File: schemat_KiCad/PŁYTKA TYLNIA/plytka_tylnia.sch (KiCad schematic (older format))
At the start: 58 parts, among them J1 CONN_01X04, J2 PIN8, J3 PIN8, P1 USB_OTG

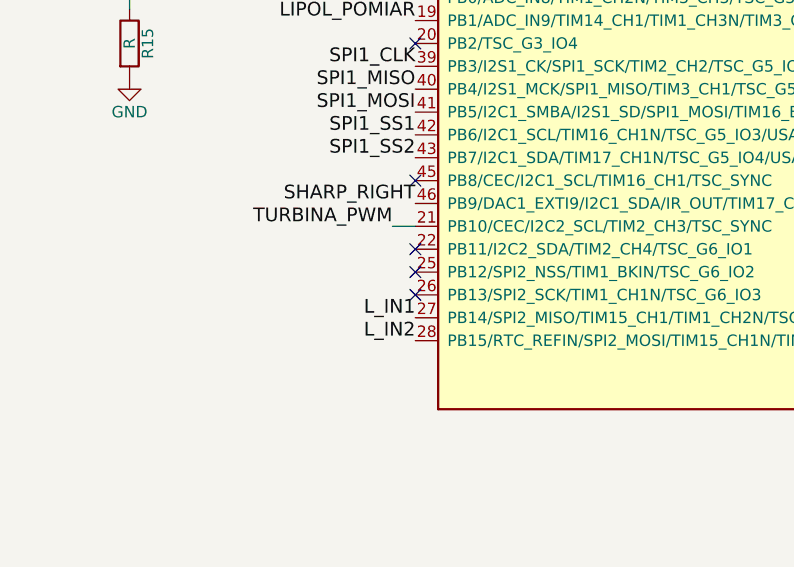
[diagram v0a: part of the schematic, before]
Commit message: kondensatory spolaryzowane na tantalowe
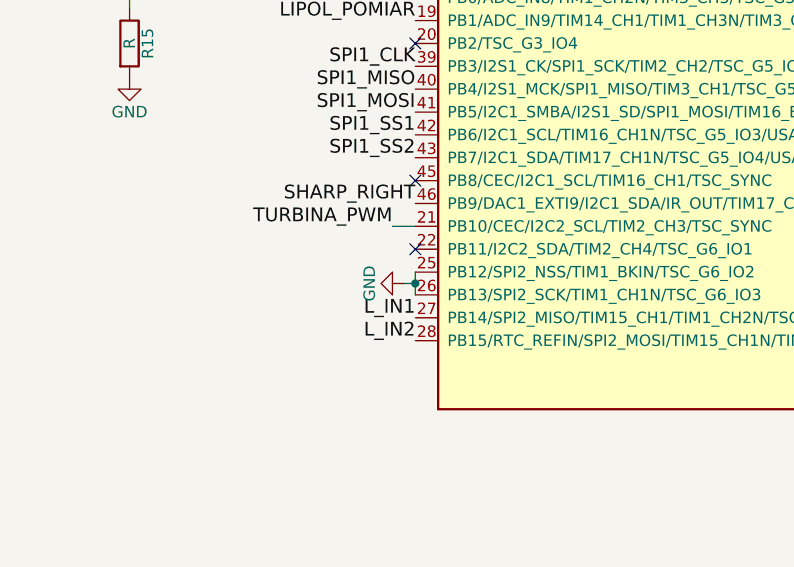
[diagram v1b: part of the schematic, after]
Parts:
- C1, C10, C14, C15, C16, C7, C8, C9: footprint Capacitors_SMD:C_0805_HandSoldering -> Capacitors_Tantalum_SMD:CP_Tantalum_Case-A_EIA-3216-18_Hand
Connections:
- net GND: now also MIKROPROCEK1.25 (PB12/SPI2_NSS/TIM1_BKIN/TSC_G6_IO2), MIKROPROCEK1.26 (PB13/SPI2_SCK/TIM1_CH1N/TSC_G6_IO3)
- no-connect marks 8 -> 6
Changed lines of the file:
@@
 F 0 "C7" H 5675 1200 50  0000 L CNN
 F 1 "4,7uF" H 5675 1000 50  0000 L CNN
-F 2 "Capacitors_SMD:C_0805_HandSoldering" H 5688 950 50  0001 C CNN
+F 2 "Capacitors_Tantalum_SMD:CP_Tantalum_Case-A_EIA-3216-18_Hand" H 5688 950 50  0001 C CNN
 F 3 "" H 5650 1100 50  0000 C CNN
 	1    5650 1100
@@
 F 0 "C10" H 12975 1250 50  0000 L CNN
 F 1 "1uF" H 12975 1050 50  0000 L CNN
-F 2 "Capacitors_SMD:C_0805_HandSoldering" H 12988 1000 50  0001 C CNN
+F 2 "Capacitors_Tantalum_SMD:CP_Tantalum_Case-A_EIA-3216-18_Hand" H 12988 1000 50  0001 C CNN
 F 3 "" H 12950 1150 50  0000 C CNN
 	1    12950 1150
@@
 F 0 "C9" H 15125 8200 50  0000 L CNN
 F 1 "10uF" H 15125 8000 50  0000 L CNN
-F 2 "Capacitors_SMD:C_0805_HandSoldering" H 15138 7950 50  0001 C CNN
+F 2 "Capacitors_Tantalum_SMD:CP_Tantalum_Case-A_EIA-3216-18_Hand" H 15138 7950 50  0001 C CNN
 F 3 "" H 15100 8100 50  0000 C CNN
 	1    15100 8100
@@
 F 0 "C8" H 14025 8250 50  0000 L CNN
 F 1 "10uF" H 14025 8050 50  0000 L CNN
-F 2 "Capacitors_SMD:C_0805_HandSoldering" H 14038 8000 50  0001 C CNN
+F 2 "Capacitors_Tantalum_SMD:CP_Tantalum_Case-A_EIA-3216-18_Hand" H 14038 8000 50  0001 C CNN
 F 3 "" H 14000 8150 50  0000 C CNN
 	1    14000 8150
@@
 F 0 "C14" H 15325 1350 50  0000 L CNN
 F 1 "10uF" H 15325 1150 50  0000 L CNN
-F 2 "Capacitors_SMD:C_0805_HandSoldering" H 15338 1100 50  0001 C CNN
+F 2 "Capacitors_Tantalum_SMD:CP_Tantalum_Case-A_EIA-3216-18_Hand" H 15338 1100 50  0001 C CNN
 F 3 "" H 15300 1250 50  0000 C CNN
 	1    15300 1250
@@
 F 0 "C16" H 15125 6950 50  0000 L CNN
 F 1 "10uF" H 15125 6750 50  0000 L CNN
-F 2 "Capacitors_SMD:C_0805_HandSoldering" H 15138 6700 50  0001 C CNN
+F 2 "Capacitors_Tantalum_SMD:CP_Tantalum_Case-A_EIA-3216-18_Hand" H 15138 6700 50  0001 C CNN
 F 3 "" H 15100 6850 50  0000 C CNN
 	1    15100 6850
@@
 F 0 "C15" H 14025 7000 50  0000 L CNN
 F 1 "10uF" H 14025 6800 50  0000 L CNN
-F 2 "Capacitors_SMD:C_0805_HandSoldering" H 14038 6750 50  0001 C CNN
+F 2 "Capacitors_Tantalum_SMD:CP_Tantalum_Case-A_EIA-3216-18_Hand" H 14038 6750 50  0001 C CNN
 F 3 "" H 14000 6900 50  0000 C CNN
 	1    14000 6900
@@
 F 0 "C1" H 5275 1200 50  0000 L CNN
 F 1 "4,7uF" H 5275 1000 50  0000 L CNN
-F 2 "Capacitors_SMD:C_0805_HandSoldering" H 5288 950 50  0001 C CNN
+F 2 "Capacitors_Tantalum_SMD:CP_Tantalum_Case-A_EIA-3216-18_Hand" H 5288 950 50  0001 C CNN
 F 3 "" H 5250 1100 50  0000 C CNN
 	1    5250 1100
@@
 Wire Wire Line
 	3150 9900 3100 9900
-NoConn ~ 2200 5350
-NoConn ~ 2200 5450
 NoConn ~ 2200 4350
 Text Label 2100 5150 2    60   ~ 0
@@
 Wire Wire Line
 	12000 7900 12000 8500
+Wire Wire Line
+	2200 5350 2200 5450
+Wire Wire Line
+	2200 5400 2150 5400
+Connection ~ 2200 5400
+$Comp
+L GND #PWR?
+U 1 1 5910F31F
+P 2150 5400
+F 0 "#PWR?" H 2150 5150 50  0001 C CNN
+F 1 "GND" H 2150 5250 50  0000 C CNN
+F 2 "" H 2150 5400 50  0001 C CNN
+F 3 "" H 2150 5400 50  0001 C CNN
+	1    2150 5400
+	0    1    1    0
+$EndComp
 $EndSCHEMATC

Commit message: skompletowane czesci, wybrane rezystory, kondensator przy wejsciu
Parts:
- added C18: 100nF, Capacitors_SMD:C_0805_HandSoldering, symbol C
- C10: value 1uF -> 10uF
- C11: value 10uF -> 100nF
- C13: value 0.1uF -> 100nF
- R10: value R -> 220R
- R11: value R -> 43k
- R12: value R -> 13k
- R13: value R -> 56k
- R14: value R -> 51k
- R15: value R -> 33k
- R4: value R -> 160k
- R5: value R -> 20k
- R9: value R -> 10k
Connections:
- net GND: now also C18.2
- net VCC: now also C18.1
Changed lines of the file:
@@
 P 13200 1150
 F 0 "C11" H 13225 1250 50  0000 L CNN
-F 1 "10uF" H 13225 1050 50  0000 L CNN
+F 1 "100nF" H 13225 1050 50  0000 L CNN
 F 2 "Capacitors_SMD:C_0805_HandSoldering" H 13238 1000 50  0001 C CNN
 F 3 "" H 13200 1150 50  0000 C CNN
@@
 P 12950 1150
 F 0 "C10" H 12975 1250 50  0000 L CNN
-F 1 "1uF" H 12975 1050 50  0000 L CNN
+F 1 "10uF" H 12975 1050 50  0000 L CNN
 F 2 "Capacitors_Tantalum_SMD:CP_Tantalum_Case-A_EIA-3216-18_Hand" H 12988 1000 50  0001 C CNN
 F 3 "" H 12950 1150 50  0000 C CNN
@@
 L VCC #PWR07
 U 1 1 5825FE4C
-P 1750 9800
-F 0 "#PWR07" H 1750 9650 50  0001 C CNN
-F 1 "VCC" H 1750 9950 50  0000 C CNN
-F 2 "" H 1750 9800 50  0000 C CNN
-F 3 "" H 1750 9800 50  0000 C CNN
-	1    1750 9800
+P 1550 9550
+F 0 "#PWR07" H 1550 9400 50  0001 C CNN
+F 1 "VCC" H 1550 9700 50  0000 C CNN
+F 2 "" H 1550 9550 50  0000 C CNN
+F 3 "" H 1550 9550 50  0000 C CNN
+	1    1550 9550
 	1    0    0    -1
 $EndComp
@@
 P 14850 1250
 F 0 "C13" H 14875 1350 50  0000 L CNN
-F 1 "0.1uF" H 14875 1150 50  0000 L CNN
+F 1 "100nF" H 14875 1150 50  0000 L CNN
 F 2 "Capacitors_SMD:C_0805_HandSoldering" H 14888 1100 50  0001 C CNN
 F 3 "" H 14850 1250 50  0000 C CNN
@@
 	1550 9900 2100 9900
 Wire Wire Line
-	1750 9800 1550 9800
-Wire Wire Line
 	12550 1300 12550 1100
 Wire Wire Line
@@
 P 9950 1750
 F 0 "R10" V 10030 1750 50  0000 C CNN
-F 1 "R" V 9950 1750 50  0000 C CNN
+F 1 "220R" V 9950 1750 50  0000 C CNN
 F 2 "Resistors_SMD:R_0805_HandSoldering" V 9880 1750 50  0001 C CNN
 F 3 "" H 9950 1750 50  0001 C CNN
@@
 P 10850 1400
 F 0 "R11" V 10930 1400 50  0000 C CNN
-F 1 "R" V 10850 1400 50  0000 C CNN
+F 1 "43k" V 10850 1400 50  0000 C CNN
 F 2 "Resistors_SMD:R_0805_HandSoldering" V 10780 1400 50  0001 C CNN
 F 3 "" H 10850 1400 50  0001 C CNN
@@
 P 10850 1700
 F 0 "R12" V 10930 1700 50  0000 C CNN
-F 1 "R" V 10850 1700 50  0000 C CNN
+F 1 "13k" V 10850 1700 50  0000 C CNN
 F 2 "Resistors_SMD:R_0805_HandSoldering" V 10780 1700 50  0001 C CNN
 F 3 "" H 10850 1700 50  0001 C CNN
@@
 P 10850 2150
 F 0 "R13" V 10930 2150 50  0000 C CNN
-F 1 "R" V 10850 2150 50  0000 C CNN
+F 1 "56k" V 10850 2150 50  0000 C CNN
 F 2 "Resistors_SMD:R_0805_HandSoldering" V 10780 2150 50  0001 C CNN
 F 3 "" H 10850 2150 50  0001 C CNN
@@
 P 10850 2000
 F 0 "R9" V 10930 2000 50  0000 C CNN
-F 1 "R" V 10850 2000 50  0000 C CNN
+F 1 "10k" V 10850 2000 50  0000 C CNN
 F 2 "Resistors_SMD:R_0805_HandSoldering" V 10780 2000 50  0001 C CNN
 F 3 "" H 10850 2000 50  0001 C CNN
@@
 P 10850 1850
 F 0 "R5" V 10930 1850 50  0000 C CNN
-F 1 "R" V 10850 1850 50  0000 C CNN
+F 1 "20k" V 10850 1850 50  0000 C CNN
 F 2 "Resistors_SMD:R_0805_HandSoldering" V 10780 1850 50  0001 C CNN
 F 3 "" H 10850 1850 50  0001 C CNN
@@
 P 10850 1550
 F 0 "R4" V 10930 1550 50  0000 C CNN
-F 1 "R" V 10850 1550 50  0000 C CNN
+F 1 "160k" V 10850 1550 50  0000 C CNN
 F 2 "Resistors_SMD:R_0805_HandSoldering" V 10780 1550 50  0001 C CNN
 F 3 "" H 10850 1550 50  0001 C CNN
@@
 P 950 4000
 F 0 "R14" V 1030 4000 50  0000 C CNN
-F 1 "R" V 950 4000 50  0000 C CNN
+F 1 "51k" V 950 4000 50  0000 C CNN
 F 2 "Resistors_SMD:R_0805_HandSoldering" V 880 4000 50  0001 C CNN
 F 3 "" H 950 4000 50  0001 C CNN
@@
 P 950 4350
 F 0 "R15" V 1030 4350 50  0000 C CNN
-F 1 "R" V 950 4350 50  0000 C CNN
+F 1 "33k" V 950 4350 50  0000 C CNN
 F 2 "Resistors_SMD:R_0805_HandSoldering" V 880 4350 50  0001 C CNN
 F 3 "" H 950 4350 50  0001 C CNN
@@
 Connection ~ 2200 5400
 $Comp
-L GND #PWR?
+L GND #PWR048
 U 1 1 5910F31F
 P 2150 5400
-F 0 "#PWR?" H 2150 5150 50  0001 C CNN
+F 0 "#PWR048" H 2150 5150 50  0001 C CNN
 F 1 "GND" H 2150 5250 50  0000 C CNN
 F 2 "" H 2150 5400 50  0001 C CNN
@@
 	0    1    1    0
 $EndComp
+Wire Wire Line
+	1550 9550 1550 9800
+$Comp
+L C C18
+U 1 1 59126A1F
+P 1700 9750
+F 0 "C18" H 1725 9850 50  0000 L CNN
+F 1 "100nF" H 1725 9650 50  0000 L CNN
+F 2 "Capacitors_SMD:C_0805_HandSoldering" H 1738 9600 50  0001 C CNN
+F 3 "" H 1700 9750 50  0001 C CNN
+	1    1700 9750
+	1    0    0    -1
+$EndComp
+Wire Wire Line
+	1700 9600 1550 9600
+Connection ~ 1550 9600
+Connection ~ 1700 9900
 $EndSCHEMATC
